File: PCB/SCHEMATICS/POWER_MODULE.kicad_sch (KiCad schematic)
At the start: 22 parts, among them U2 AMS1117-3.3

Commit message: Updated schematics
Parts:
- added C22808: 150, symbol Device:R_Small_US
- C25867: renamed from R1; value 1.65k -> 1.5k
- renumbered C4 to C28323
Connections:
- net at C25867.1: now also C22808.2; no longer C32574.5 (Prog)
- new net: C22808.1, C32574.5 (Prog)
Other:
- company: (none) -> UCT
- moved on the sheet: C25867
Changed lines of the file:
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@@
   (title_block
     (title "POWER MODULE")
+    (rev "11/03/2023")
+    (company "UCT")
+    (comment 1 "Author: Tinashe Timba")
+    (comment 2 "Version: 2")
   )
   (junction (at 224.79 99.06) (diameter 0) (color 0 0 0 0)
@@
   )
   (wire (pts (xy 212.09 68.58) (xy 199.39 68.58))
+    (stroke (width 0) (type default))
+  )
+  (wire (pts (xy 90.17 86.36) (xy 90.17 90.17))
     (stroke (width 0) (type default))
   )
@@
     )
   )
-  (symbol (lib_id "Device:R_Small_US") (at 90.17 83.82 0) (unit 1)
-    (in_bom yes) (on_board yes) (dnp no) (fields_autoplaced)
-    (property "Reference" "R1" (at 92.71 83.185 0)
-      (effects (font (size 1.27 1.27)) (justify left))
-    )
-    (property "Value" "1.65k" (at 92.71 85.725 0)
-      (effects (font (size 1.27 1.27)) (justify left))
-    )
-    (property "Footprint" "" (at 90.17 83.82 0)
-      (effects (font (size 1.27 1.27)) hide)
-    )
-    (property "Datasheet" "~" (at 90.17 83.82 0)
+  (symbol (lib_id "Device:R_Small_US") (at 90.17 92.71 0) (unit 1)
+    (in_bom yes) (on_board yes) (dnp no) (fields_autoplaced)
+    (property "Reference" "C25867" (at 92.71 92.075 0)
+      (effects (font (size 1.27 1.27)) (justify left))
+    )
+    (property "Value" "1.5k" (at 92.71 94.615 0)
+      (effects (font (size 1.27 1.27)) (justify left))
+    )
+    (property "Footprint" "" (at 90.17 92.71 0)
+      (effects (font (size 1.27 1.27)) hide)
+    )
+    (property "Datasheet" "~" (at 90.17 92.71 0)
       (effects (font (size 1.27 1.27)) hide)
     )
@@
       (project "SCHEMATICS"
         (path "/c9ca3a5c-30cb-4dce-b611-3270b9f3284b/c574ee02-103d-4bad-a8c0-5ec1707f609e"
-          (reference "R1") (unit 1)
-        )
-      )
-    )
-  )
-  (symbol (lib_id "power:GND") (at 90.17 86.36 0) (unit 1)
-    (in_bom yes) (on_board yes) (dnp no) (fields_autoplaced)
-    (property "Reference" "#PWR023" (at 90.17 92.71 0)
-      (effects (font (size 1.27 1.27)) hide)
-    )
-    (property "Value" "GND" (at 90.17 91.44 0)
+          (reference "C25867") (unit 1)
+        )
+      )
+    )
+  )
+  (symbol (lib_id "power:GND") (at 90.17 95.25 0) (unit 1)
+    (in_bom yes) (on_board yes) (dnp no) (fields_autoplaced)
+    (property "Reference" "#PWR023" (at 90.17 101.6 0)
+      (effects (font (size 1.27 1.27)) hide)
+    )
+    (property "Value" "GND" (at 90.17 100.33 0)
       (effects (font (size 1.27 1.27)))
     )
-    (property "Footprint" "" (at 90.17 86.36 0)
-      (effects (font (size 1.27 1.27)) hide)
-    )
-    (property "Datasheet" "" (at 90.17 86.36 0)
+    (property "Footprint" "" (at 90.17 95.25 0)
+      (effects (font (size 1.27 1.27)) hide)
+    )
+    (property "Datasheet" "" (at 90.17 95.25 0)
       (effects (font (size 1.27 1.27)) hide)
     )
@@
   (symbol (lib_id "Device:C_Small") (at 60.96 68.58 0) (unit 1)
     (in_bom yes) (on_board yes) (dnp no) (fields_autoplaced)
-    (property "Reference" "C4" (at 63.5 67.9513 0)
+    (property "Reference" "C28323" (at 63.5 67.9513 0)
       (effects (font (size 1.27 1.27)) (justify left))
     )
@@
       (project "SCHEMATICS"
         (path "/c9ca3a5c-30cb-4dce-b611-3270b9f3284b/c574ee02-103d-4bad-a8c0-5ec1707f609e"
-          (reference "C4") (unit 1)
+          (reference "C28323") (unit 1)
         )
       )
@@
         )
       )
+    )
+  )
+  (symbol (lib_id "Device:R_Small_US") (at 90.17 83.82 0) (unit 1)
+    (in_bom yes) (on_board yes) (dnp no) (fields_autoplaced)
+    (property "Reference" "C22808" (at 92.71 83.185 0)
+      (effects (font (size 1.27 1.27)) (justify left))
+    )
+    (property "Value" "150" (at 92.71 85.725 0)
+      (effects (font (size 1.27 1.27)) (justify left))
+    )
+    (property "Footprint" "" (at 90.17 83.82 0)
+      (effects (font (size 1.27 1.27)) hide)
+    )
+    (property "Datasheet" "~" (at 90.17 83.82 0)
+      (effects (font (size 1.27 1.27)) hide)
+    )
+    (pin "1")
+    (pin "2")
+    (instances
+      (project "SCHEMATICS"
+        (path "/c9ca3a5c-30cb-4dce-b611-3270b9f3284b/c574ee02-103d-4bad-a8c0-5ec1707f609e"
+          (reference "C22808") (unit 1)
+        )
+      )

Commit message: Updated schematics
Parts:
- removed C8062: D_Zener, symbol Device:D_Zener
- removed TP11, TP12: TestPoint, symbol Connector:TestPoint
- removed V1: ~, symbol Simulation_SPICE:VDC
- added C1: D_Schottky, symbol Device:D_Schottky
- added C4177 (x6): 0, symbol Device:R_Small_US
- added D1: D_Zener, symbol Device:D_Zener
- added Q1: PMOS, symbol Simulation_SPICE:PMOS
- added R1, R2, R3, R4, R5, R6: R_Small_US, symbol Device:R_Small_US
- added U1: AD8603, Package_TO_SOT_SMD:TSOT-23-5, symbol Amplifier_Operational:AD8603
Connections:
- net 5V: now also C4177.1; no longer C191023.2 (A), TP9.1
- net Battery: now also C4177.1, C4177.2; no longer C191023.2 (A), C32574.3 (BATT), TP4.1, TP5.1
- net GND: now also C4177.1
- new net: R1.2, R2.1, U1.4 (-)
- new net: C1.1 (K), Q1.3 (S), R1.1, R2.2, R3.1, R4.2, U1.2 (V-), U1.5 (V+)
- new net: C191023.2 (A), C4177.2, TP5.1
- new net: C191023.2 (A), C4177.2, TP9.1
- new net: C4177.1, Q1.1 (D)
- new net: D1.2 (A), R4.1, R6.2
- new net: C32574.3 (BATT), C4177.1, TP4.1
- new net: Q1.2 (G), R5.1
- new net: C1.2 (A), C4177.2
- new net: R5.2, R6.1, U1.1
- new net: D1.1 (K), R3.2, U1.3 (+)
- new net 3V3: C4177.2
- new net UVLO Output: C4177.1, C4177.2
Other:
- note added: "Under Voltage Lockout Circuit"

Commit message: Updated BOM
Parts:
- added R40: Value: Value: Value: Value: Value: 510k, symbol Device:R_Small_US
- C1: renamed from C28323; PART  (none) -> C28323; Unit Price (none) -> 0.0058
- C2, C3: renamed from C19702; PART  (none) -> C19702
- D1: renamed from C191023; PART  (none) -> C191023; Unit Price (none) -> 0.0167
- D2: renamed from C95872; PART  (none) -> C95872
- D3: renamed from D1; PART  (none) -> C8056; Unit Price (none) -> 0.0111
- D4: renamed from C191023; PART  (none) -> C191023
- D5: renamed from C1; PART  (none) -> C191023
- Q1: PART  (none) -> C20917; Unit Price (none) -> 0.0864
- R1, R14, R15, R4, R5, R7: renamed from C4177; PART  (none) -> C4177; Unit Price (none) -> 0.0012
- R10: renamed from R2; value R_Small_US -> 3M; PART  (none) -> C23156; Unit Price (none) -> 0.0013
- R11: renamed from R4; value R_Small_US -> 150k; PART  (none) -> C22807; Unit Price (none) -> 0.0010
- R12: renamed from R5; value R_Small_US -> 1M; PART  (none) -> C17927; Unit Price (none) -> 0.0031
- R13: renamed from R6; value R_Small_US -> 10M; PART  (none) -> C26108; Unit Price (none) -> 0.0024
- R2: renamed from C22808; PART  (none) -> C22808; Unit Price (none) -> 0.0010
- R3: renamed from C25867; PART  (none) -> C25867; Unit Price (none) -> 0.0005
- R6: renamed from C17520; PART  (none) -> C17520
- R8: renamed from R1; value R_Small_US -> 3M; PART  (none) -> C23156; Unit Price (none) -> 0.0013
- R9: renamed from R3; value R_Small_US -> 2.0M; PART  (none) -> C22976; Unit Price (none) -> 0.0016
- TP10: PART  (none) -> TP10
- TP3: PART  (none) -> TP3
- TP4: PART  (none) -> TP4
- TP4054-42-SOT25R: renamed from C32574; PART  (none) -> C32574; Unit Price (none) -> 0.1433
- TP5: PART  (none) -> TP5
- TP6: PART  (none) -> TP6
- TP7: PART  (none) -> TP7
- TP8: PART  (none) -> TP8
- TP9: PART  (none) -> TP9
- U1: value AD8603 -> C7433; PART  (none) -> C7433; Unit Price (none) -> 0.2804
- U2: PART  (none) -> U2
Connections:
- net at R10.1, U1.4 (-): now also R40.2; no longer R8.2
- new net: R40.1, R8.2

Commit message: Updating schematics
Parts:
- added TP11, TP12, TP28, TP29, TP30, TP31: TestPoint, symbol Connector:TestPoint
- added U4: AMS1117-3.3, Package_TO_SOT_SMD:SOT-223-3_TabPin2, symbol Regulator_Linear:AMS1117-3.3
- R40: value Value: Value: Value: Value: Value: 510k -> 510k
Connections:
- net Battery: now also TP30.1
- net GND: now also TP29.1
- net UVLO Output: now also TP31.1
- new net: TP28.1, U4.3 (VI)
- new net: TP11.1, U4.2 (VO)
- new net: TP12.1, U4.1 (GND)
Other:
- note added: "Spare 3V3 Regulator"
- moved on the sheet: C1, C2, C3, D1, D2, D3, D4, D5, Q1, R1, R10, R11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

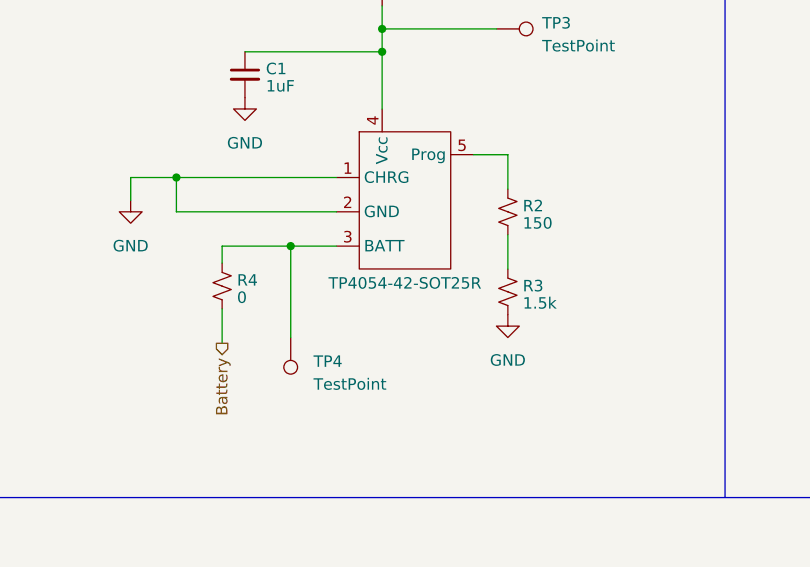
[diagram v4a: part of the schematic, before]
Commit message: added footprints
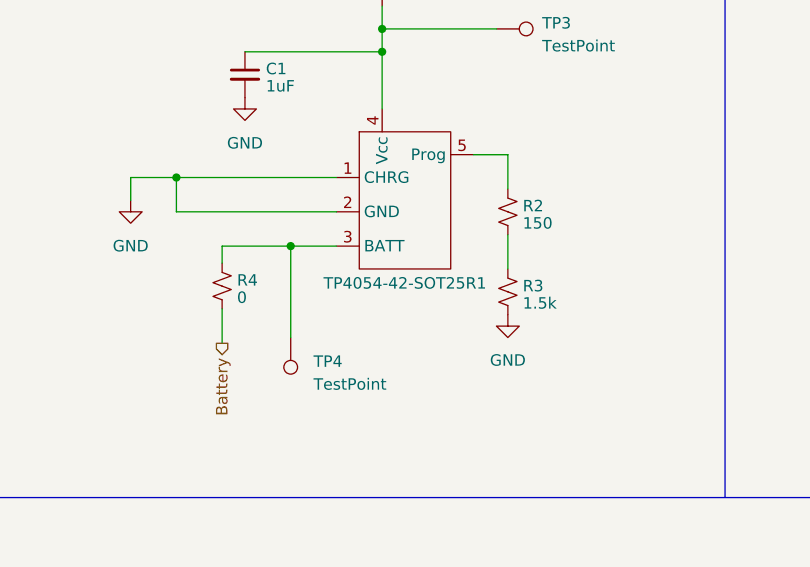
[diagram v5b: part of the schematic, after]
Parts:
- renumbered TP4054-42-SOT25R to TP4054-42-SOT25R1
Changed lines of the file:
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@@
   (symbol (lib_id "Battery charging:TP4054") (at 66.04 59.69 0) (unit 1)
     (in_bom yes) (on_board yes) (dnp no) (fields_autoplaced)
-    (property "Reference" "TP4054-42-SOT25R" (at 66.04 79.0655 0)
+    (property "Reference" "TP4054-42-SOT25R1" (at 66.04 79.0655 0)
       (effects (font (size 1.27 1.27)))
     )
@@
       (project "SCHEMATICS"
         (path "/c9ca3a5c-30cb-4dce-b611-3270b9f3284b/c574ee02-103d-4bad-a8c0-5ec1707f609e"
-          (reference "TP4054-42-SOT25R") (unit 1)
+          (reference "TP4054-42-SOT25R1") (unit 1)
         )
       )
